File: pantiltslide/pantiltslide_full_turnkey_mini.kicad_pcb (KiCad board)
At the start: 4 copper layers, 54 x 93 mm, 63 parts, among them J1 Conn_01x22_Socket, J17 Motor_Slide, J18 Motor_Pan, J19 Motor_Tilt, J2 Conn_01x22_Socket, J20 TCA9548A_Mux, J21 AS5600_Pan, J22 AS5600_Tilt, J23 OLED, J24 TCA9548A_Mux, J26 Limit_Min, J27 Limit_Max, J28 Motor_Aux, J29 Enc_Slide, J3 MUX_2, J30 Enc_Pan, J31 Enc_Tilt, J32 Enc_Aux, J33 Btn_SetKeyframe, J34 Btn_ClearKeyframe, J35 Btn_PlayPause, J36 Btn_Reset, J37 5V_In, J38 24V_In, J4 MUX_3, J41 Aux_Max, J5 MUX_4, J6 MUX_5, J7 MUX_6, J8 MUX_7, U1 tmc2209, U2 tmc2209, U3 tmc2209, U4 tmc2209

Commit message: wreyh
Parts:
- moved C16 76.6 mm to (116.5, 105.0), turned to -90 degrees
- moved C15 61.5 mm to (114.0, 82.5), turned to -90 degrees
- moved C17 46.6 mm to (109.0, 77.5), turned to 180 degrees
- moved C14 36.5 mm to (114.0, 60.0), turned to -90 degrees
- moved C12 18.4 mm to (125.5, 20.0), turned to -90 degrees
- moved C13 11.6 mm to (114.5, 37.5), turned to -90 degrees
- moved R1 2.02 mm to (108.5, 75.5)
- moved R2 2.02 mm to (112.0, 75.5)
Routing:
- net VCC_5V: track 0.00 -> 30.6 mm
- net 3.3v: track 438.1 -> 462.4 mm, vias 1 -> 3
- net GPIO_42: track 18.6 -> 12.7 mm
- net GND: track 28.0 -> 30.4 mm
- net GPIO_11: track 40.9 -> 42.4 mm
- net GPIO_7: track 38.3 -> 37.5 mm
- net GPIO_4: track 28.4 -> 29.0 mm

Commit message: re wiring pcb
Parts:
- F1, U1, U2, U3, U4: moved to B.Cu
- J6, J7, J8: moved to F.Cu
- moved J8 75.2 mm to (117.6, 88.6), turned to 90 degrees
- moved J7 68.0 mm to (117.6, 92.7), turned to 90 degrees
- moved C13 65.0 mm to (101.1, 101.1)
- moved J6 61.2 mm to (117.6, 96.8), turned to 90 degrees
- moved J17 51.6 mm to (92.4, 71.8), turned to 90 degrees
- moved C8 49.9 mm to (101.9, 20.1)
- moved U3 49.6 mm to (98.3, 37.8), turned to 0 degrees
- moved J19 49.1 mm to (92.5, 36.8), turned to 90 degrees
- moved C15 48.8 mm to (101.4, 35.3), turned to 0 degrees
- moved F1 48.5 mm to (90.8, 107.2), turned to 0 degrees
- moved C2 48.0 mm to (103.5, 67.6)
- moved J21 47.7 mm to (135.1, 90.0), turned to -90 degrees
- moved C6 47.3 mm to (102.2, 63.2)
- moved C4 46.8 mm to (102.0, 25.4)
- moved U1 46.0 mm to (98.3, 80.9), turned to 0 degrees
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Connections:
- J3 pad 2: unconnected-(J3-Pin_2-Pad2) -> GND
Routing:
- net 3.3v: track 462.4 -> 225.3 mm, vias 3 -> 2
- net MUX_CH7_SDA: track 62.7 -> 11.5 mm
- net MUX_CH7_SCL: track 61.0 -> 17.0 mm
- net GPIO_5: track 28.4 -> 72.4 mm
- net MUX_CH6_SDA: track 56.7 -> 13.3 mm
- net +24V: track 143.2 -> 100.6 mm
- net MUX_CH6_SCL: track 52.5 -> 15.6 mm
- net GPIO_4: track 29.0 -> 64.0 mm
- net MUX_CH5_SDA: track 45.6 -> 11.9 mm
- net MUX_CH5_SCL: track 46.4 -> 14.6 mm
- net GND: track 30.4 -> 2.54 mm, vias 0 -> 11
- net MUX_CH2_SCL: track 38.9 -> 11.9 mm
- net GPIO_1: track 83.3 -> 109.0 mm
- net GPIO_21: track 8.42 -> 34.0 mm
- net GPIO_19: track 6.86 -> 31.9 mm
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- added copper zone on F.Cu, net +24V
- added copper zone on F.Cu, net 3.3v
- removed copper zone on B.Cu, net +24V
- removed copper zone on B.Cu, net VCC_5V
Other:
- board size 54 x 93 mm -> 52.3 x 93.2 mm

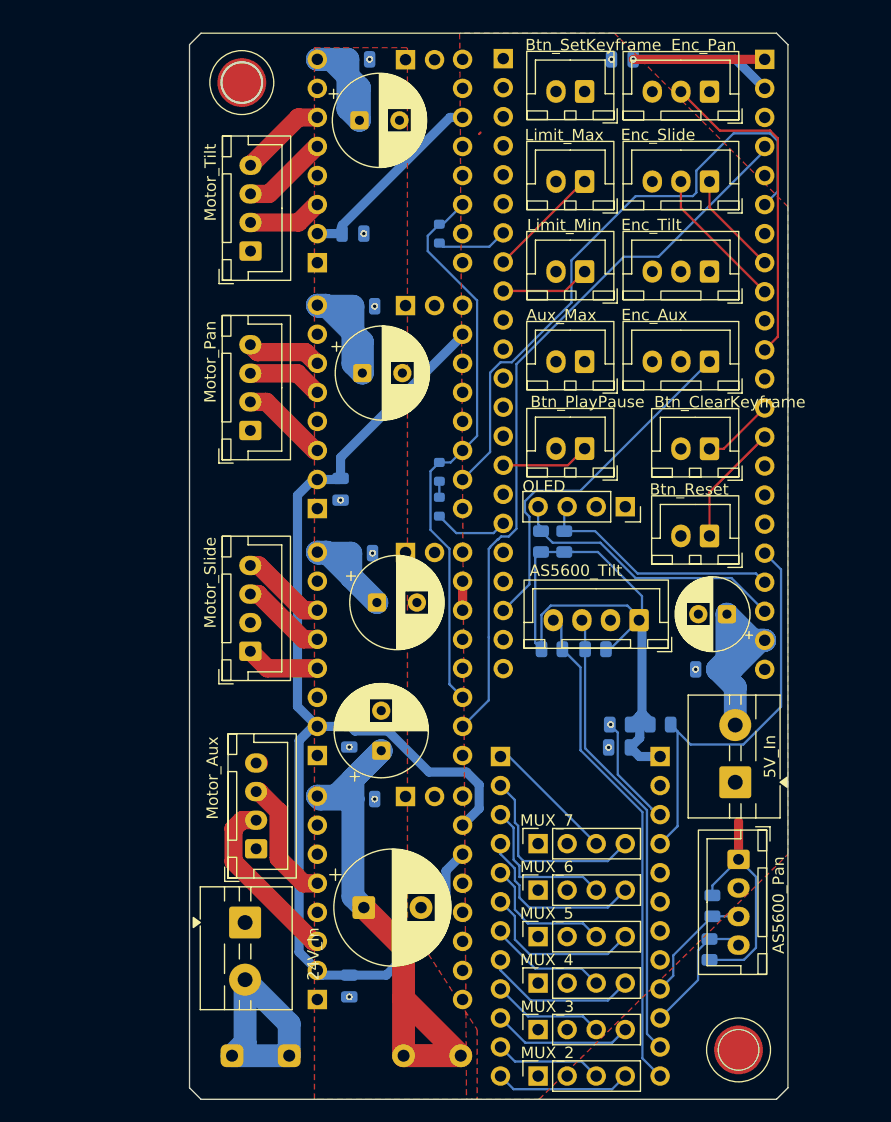
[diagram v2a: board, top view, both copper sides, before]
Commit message: updates to the pcb wiring
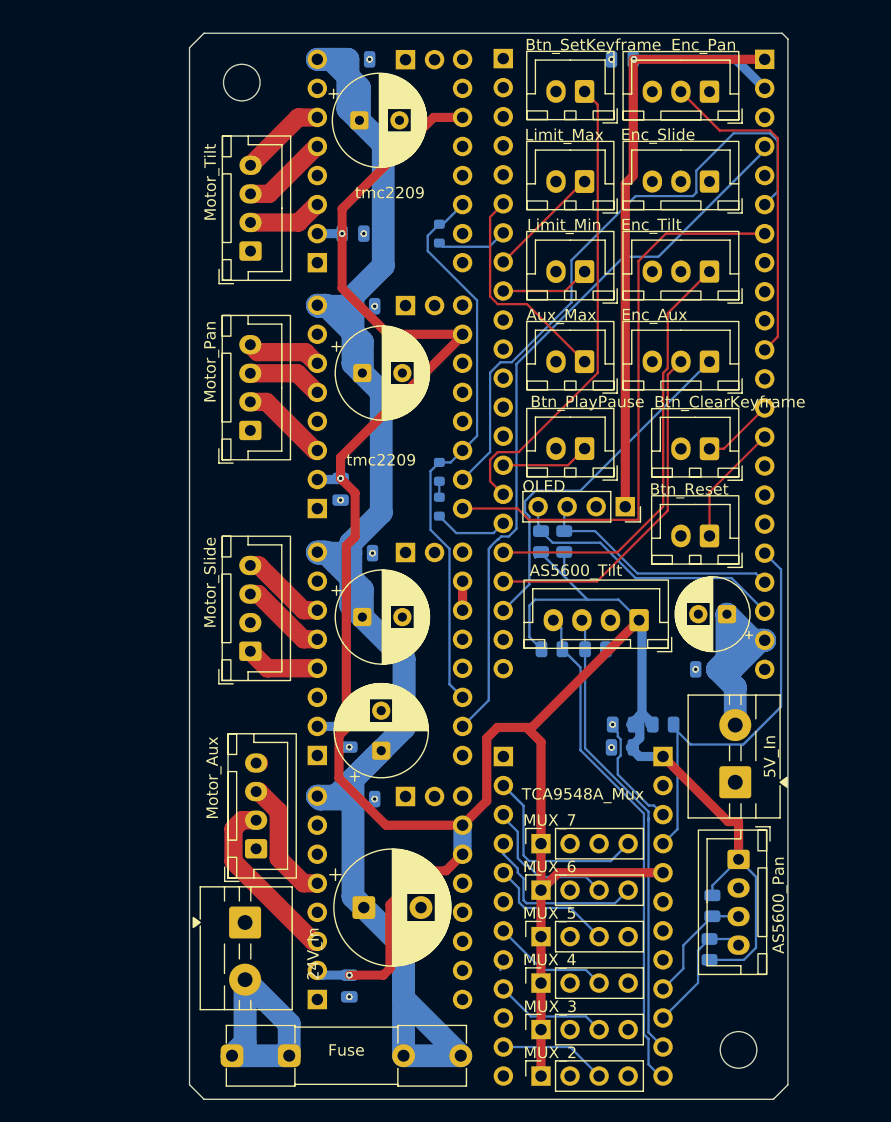
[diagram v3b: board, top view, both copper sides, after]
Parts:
- added REF**: MountingHole_3.2mm_M3, MountingHole:MountingHole_3.2mm_M3, F.Cu at (135.1, 106.7)
- added REF**: MountingHole_3.2mm_M3, MountingHole:MountingHole_3.2mm_M3, F.Cu at (91.7, 22.1)
- F1: moved to F.Cu
- moved C2 1.80 mm to (102.2, 68.8)
- moved J24 0.25 mm to (114.6, 81.0)
- moved R1 0.25 mm to (125.0, 78.2)
- moved C17 0.25 mm to (125.0, 80.2)
- moved J20 0.25 mm to (128.5, 81.0)
- moved J3 0.25 mm to (117.9, 109.0)
- moved J4 0.25 mm to (117.9, 104.9)
- moved J5 0.25 mm to (117.9, 100.8)
- moved J6 0.25 mm to (117.9, 96.8)
- moved J7 0.25 mm to (117.9, 92.7)
- moved J8 0.25 mm to (117.9, 88.6)
- moved R2 0.25 mm to (128.5, 78.2)
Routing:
- net 3.3v: track 225.3 -> 339.6 mm, vias 2 -> 6
- net +24V: track 100.6 -> 157.1 mm
- net GPIO_7: track 41.5 -> 50.4 mm
- net GPIO_21: track 34.0 -> 37.9 mm
- net GPIO_20: track 27.5 -> 30.5 mm
- net MUX_CH5_SCL: track 14.6 -> 12.2 mm
- net GPIO_42: track 16.7 -> 19.2 mm
- net GPIO_48: track 39.1 -> 41.1 mm
- net GPIO_12: track 37.1 -> 35.3 mm
- net MUX_CH4_SCL: track 13.5 -> 12.7 mm
- net GPIO_11: track 32.9 -> 33.7 mm
- net MUX_CH7_SDA: track 11.5 -> 12.3 mm
- net GPIO_1: track 109.0 -> 108.4 mm
- net MUX_CH1_SDA: track 40.0 -> 40.7 mm
- net MUX_CH6_SDA: track 13.3 -> 12.7 mm
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- added copper zone on In1.Cu, net GND
- removed copper zone on F.Cu, net +24V
- removed copper zone on F.Cu, net 3.3v
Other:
- outline, holes or cut-outs redrawn

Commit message: perfect finished locked and sent to pcbway
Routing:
- net 3.3v: track 339.6 -> 380.8 mm
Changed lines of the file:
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@@
 			(drillshape 0)
 			(scaleselection 1)
-			(outputdirectory "../../../Downloads/New folder (2)/")
+			(outputdirectory "C:/Users/acard/Downloads/turnkey_mini/")
 		)
 	)
@@
 		)
 		(property "Value" "tmc2209"
-			(at 6.35 -6.096 -0)
+			(at 6.35 -6.096 0)
 			(layer "F.SilkS")
 			(effects
@@
 		)
 		(property "Value" "TCA9548A_Mux"
-			(at -6.9588 -3.302 -0)
+			(at -6.9588 -3.302 0)
 			(layer "F.SilkS")
 			(effects
@@
 		)
 		(property "Value" "tmc2209"
-			(at 5.588 -4.227905 -180)
+			(at 5.588 -4.227905 180)
 			(layer "F.SilkS")
 			(effects
@@
 	)
 	(segment
+		(start 133.9615 91.186)
+		(end 135.128 90.0195)
+		(width 0.8)
+		(layer "F.Cu")
+		(net "3.3v")
+	)
+	(segment
 		(start 117.856 108.966)
 		(end 117.856 104.902)
@@
 	)
 	(segment
+		(start 131.318 76.454)
+		(end 131.318 83.312)
+		(width 0.8)
+		(layer "F.Cu")
+		(net "3.3v")
+	)
+	(segment
 		(start 100.462 40.078793)
 		(end 100.462 35.306)
@@
 	(segment
 		(start 134.2155 86.7175)
-		(end 128.524 81.026)
+		(end 131.064 83.566)
 		(width 0.8)
 		(layer "F.Cu")
@@
 	)
 	(segment
+		(start 110.998 24.469654)
+		(end 110.998 25.146)
+		(width 0.2)
+		(layer "F.Cu")
+		(net "3.3v")
+	)
+	(segment
 		(start 110.998 87.031906)
 		(end 111.462094 87.496)
@@
 	)
 	(segment
+		(start 125.984 20.066)
+		(end 124.714 21.336)
+		(width 0.2)
+		(layer "F.Cu")
+		(net "3.3v")
+	)
+	(segment
 		(start 116.586 78.486)
 		(end 117.051 78.486)
@@
 	)
 	(segment
+		(start 126.432 69.105)
+		(end 126.432 71.568)
+		(width 0.8)
+		(layer "F.Cu")
+		(net "3.3v")
+	)
+	(segment
 		(start 104.489112 44.105905)
 		(end 100.462 40.078793)
@@
 	)
 	(segment
+		(start 131.064 83.566)
+		(end 128.524 81.026)
+		(width 0.8)
+		(layer "F.Cu")
+		(net "3.3v")
+	)
+	(segment
 		(start 108.458 25.146)
 		(end 110.998 25.146)
@@
 	)
 	(segment
+		(start 124.714 21.336)
+		(end 114.131654 21.336)
+		(width 0.2)
+		(layer "F.Cu")
+		(net "3.3v")
+	)
+	(segment
+		(start 128.524 91.186)
+		(end 133.9615 91.186)
+		(width 0.8)
+		(layer "F.Cu")
+		(net "3.3v")
+	)
+	(segment
 		(start 110.998 87.031906)
 		(end 113.1152 84.914706)
@@
 	)
 	(segment
+		(start 131.318 83.312)
+		(end 131.064 83.566)
+		(width 0.8)
+		(layer "F.Cu")
+		(net "3.3v")
+	)
+	(segment
 		(start 98.642095 56.805905)
 		(end 98.298 56.805905)
@@
 	)
 	(segment
+		(start 114.131654 21.336)
+		(end 110.998 24.469654)
+		(width 0.2)
+		(layer "F.Cu")
+		(net "3.3v")
+	)
+	(segment
 		(start 101.092 100.142)
 		(end 104.074 100.142)
@@
 	)
 	(segment
+		(start 126.432 71.568)
+		(end 131.318 76.454)
+		(width 0.8)
+		(layer "F.Cu")
+		(net "3.3v")
+	)
+	(segment
 		(start 117.051 78.486)
 		(end 126.432 69.105)
@@
 		(start 126.432 60.392)
 		(end 125.222 59.182)
-		(width 0.8)
+		(width 1.2)
 		(layer "In2.Cu")
 		(net "3.3v")
@@
 		(start 126.432 69.105)
 		(end 126.432 60.392)
-		(width 0.8)
+		(width 1.2)
 		(layer "In2.Cu")
 		(net "3.3v")
@@
 		(hatch edge 0.5)
 		(connect_pads
-			(clearance 0.3)
+			(clearance 0.5)
 		)
-		(min_thickness 0.2)
+		(min_thickness 0.25)
 		(fill yes
-			(thermal_gap 0.2)
+			(thermal_gap 0.8)
 			(thermal_bridge_width 0.8)
 			(island_removal_mode 0)
@@
 		(polygon
 			(pts
-				(xy 138.43 100.584) (xy 129.54 100.584) (xy 129.54 110.236) (xy 118.872 110.296) (xy 111.76 104.14)
-				(xy 96.4805 103.54) (xy 87.6705 103.54) (xy 87.6705 92.04) (xy 96.847 92.044) (xy 97.282 26.416)
-				(xy 97.280234 18.288938) (xy 138.445902 18.287062)
+				(xy 138.429755 101.854) (xy 132.329832 101.853577) (xy 128.995956 110.71891) (xy 117.398669 110.783716)
+				(xy 109.626419 104.056218) (xy 96.4805 103.54) (xy 87.6705 103.54) (xy 87.6705 92.04) (xy 96.847 92.044)
+				(xy 97.282 26.416) (xy 97.280234 18.288938) (xy 138.445902 18.287062)
 			)
 		)

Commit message: updates and fixes
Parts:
- J34: value Btn_ClearKeyframe -> ClearKframe
- J35: value Btn_PlayPause -> PlayPause
- moved C14 1.78 mm to (100.3, 55.9), turned to 90 degrees
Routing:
- net 3.3v: track 380.8 -> 394.2 mm, vias 6 -> 5
- net GPIO_9: track 35.6 -> 41.1 mm
- net MUX_CH5_SCL: track 12.2 -> 15.1 mm
- net GPIO_10: track 96.3 -> 99.0 mm
- net GPIO_6: track 53.8 -> 51.5 mm
- net GPIO_5: track 72.4 -> 70.3 mm
- net GPIO_11: track 33.7 -> 35.5 mm
- net GPIO_8: track 35.7 -> 37.3 mm
- net GPIO_38: track 17.3 -> 18.7 mm
- net GPIO_15: track 9.09 -> 9.80 mm
- net MUX_CH4_SCL: track 12.7 -> 13.2 mm
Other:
- board text added: "+"
- board text added: "-"
- board text added: "24V_In"
- board text added: "3.3v"
- board text added: "4AMP"
- board text added: "5V_In"
- board text added: "AMOVFC"
- board text added: "AS5600_Pan"
- board text added: "By AMOVFC"
- board text added: "ESP32-S3"
- board text added: "GND"
- board text added: "PanTiltSlide"
- board text added: "SDA SCL"
- board text added: "VCC_5V"
- board text added: "by AMOVFC"
- board text added: "v1.0"

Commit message: new version of board with more caps and res
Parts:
- added F2: Fuseholder_Littelfuse_Nano2_154x, Fuse:Fuseholder_Littelfuse_Nano2_154x, F.Cu at (143.8, 75.2)
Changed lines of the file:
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@@
 		)
 		(property "Value" "5V_In"
-			(at 1.996 3.5885 -90)
+			(at 1.996 3.5885 270)
 			(layer "B.SilkS")
 			(effects
@@
 			(offset
 				(xyz 0 0 0)
+			)
+			(scale
+				(xyz 1 1 1)
+			)
+			(rotate
+				(xyz 0 0 0)
+			)
+		)
+	)
+	(footprint "Fuse:Fuseholder_Littelfuse_Nano2_154x"
+		(layer "F.Cu")
+		(at 143.764 75.184 90)
+		(descr "Littelfuse NANO2 holder, https://www.littelfuse.com/~/media/electronics/datasheets/fuses/littelfuse_fuse_154_154t_154l_154tl_datasheet.pdf.pdf")
+		(tags "SMD Nano2 holder")
+		(property "Reference" "F2"
+			(at 0 -3.5 90)
+			(unlocked yes)
+			(layer "F.SilkS")
+			(effects
+				(font
+					(size 1 1)
+					(thickness 0.15)
+				)
+			)
+		)
+		(property "Value" "Fuseholder_Littelfuse_Nano2_154x"
+			(at 0 3.5 90)
+			(unlocked yes)
+			(layer "F.Fab")
+			(effects
+				(font
+					(size 1 1)
+					(thickness 0.15)
+				)
+			)
+		)
+		(property "Datasheet" ""
+			(at 0 0 90)
+			(unlocked yes)
+			(layer "F.Fab")
+			(hide yes)
+			(effects
+				(font
+					(size 1.27 1.27)
+					(thickness 0.15)
+				)
+			)
+		)
+		(property "Description" ""
+			(at 0 0 90)
+			(unlocked yes)
+			(layer "F.Fab")
+			(hide yes)
+			(effects
+				(font
+					(size 1.27 1.27)
+					(thickness 0.15)
+				)
+			)
+		)
+		(attr smd)
+		(duplicate_pad_numbers_are_jumpers no)
+		(fp_line
+			(start 4.975 -2.625)
+			(end 4.975 -2.165)
+			(stroke
+				(width 0.12)
+				(type solid)
+			)
+			(layer "F.SilkS")
+		)
+		(fp_line
+			(start -4.975 -2.625)
+			(end 4.975 -2.625)
+			(stroke
+				(width 0.12)
+				(type solid)
+			)
+			(layer "F.SilkS")
+		)
+		(fp_line
+			(start -4.975 -2.625)
+			(end -4.975 -2.165)
+			(stroke
+				(width 0.12)
+				(type solid)
+			)
+			(layer "F.SilkS")
+		)
+		(fp_line
+			(start -4.975 2.165)
+			(end -4.975 2.625)
+			(stroke
+				(width 0.12)
+				(type solid)
+			)
+			(layer "F.SilkS")
+		)
+		(fp_line
+			(start 4.975 2.625)
+			(end 4.975 2.165)
+			(stroke
+				(width 0.12)
+				(type solid)
+			)
+			(layer "F.SilkS")
+		)
+		(fp_line
+			(start -4.975 2.625)
+			(end 4.975 2.625)
+			(stroke
+				(width 0.12)
+				(type solid)
+			)
+			(layer "F.SilkS")
+		)
+		(fp_line
+			(start 5.56 -2.77)
+			(end 5.56 2.77)
+			(stroke
+				(width 0.05)
+				(type solid)
+			)
+			(layer "F.CrtYd")
+		)
+		(fp_line
+			(start -5.56 -2.77)
+			(end 5.56 -2.77)
+			(stroke
+				(width 0.05)
+				(type solid)
+			)
+			(layer "F.CrtYd")
+		)
+		(fp_line
+			(start -5.56 -2.77)
+			(end -5.56 2.77)
+			(stroke
+				(width 0.05)
+				(type solid)
+			)
+			(layer "F.CrtYd")
+		)
+		(fp_line
+			(start -5.56 2.77)
+			(end 5.56 2.77)
+			(stroke
+				(width 0.05)
+				(type solid)
+			)
+			(layer "F.CrtYd")
+		)
+		(fp_line
+			(start -4.865 -2.515)
+			(end 4.865 -2.515)
+			(stroke
+				(width 0.1)
+				(type solid)
+			)
+			(layer "F.Fab")
+		)
+		(fp_line
+			(start -4.865 -2.515)
+			(end -4.865 2.515)
+			(stroke
+				(width 0.1)
+				(type solid)
+			)
+			(layer "F.Fab")
+		)
+		(fp_line
+			(start 4.865 2.515)
+			(end 4.865 -2.515)
+			(stroke
+				(width 0.1)
+				(type solid)
+			)
+			(layer "F.Fab")
+		)
+		(fp_line
+			(start -4.865 2.515)
+			(end 4.865 2.515)
+			(stroke
+				(width 0.1)
+				(type solid)
+			)
+			(layer "F.Fab")
+		)
+		(fp_text user "${REFERENCE}"
+			(at 0 0 90)
+			(layer "F.Fab")
+			(effects
+				(font
+					(size 1 1)
+					(thickness 0.15)
+				)
+			)
+		)
+		(pad "1" smd rect
+			(at -3.185 0 90)
+			(size 4.24 3.81)
+			(layers "F.Cu" "F.Mask" "F.Paste")
+		)
+		(pad "2" smd rect
+			(at 3.185 0 90)
+			(size 4.24 3.81)
+			(layers "F.Cu" "F.Mask" "F.Paste")
+		)
+		(embedded_fonts no)
+		(model "${KICAD10_3DMODEL_DIR}/Fuse.3dshapes/Fuseholder_Littelfuse_Nano2_154x.step"
+			(offset
+				(xyz 0 0 0)
